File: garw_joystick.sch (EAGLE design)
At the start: 15 parts, among them IC1 TLC339D, X1 PS-05_WL, X2 PS-08_WL

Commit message: Minot stylistic fixup
Signed-off-by: Ralf Ramsauer <ralf@vmexit.de>
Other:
- note added: "Upper threshold: ~11.33V VCC - 1k3 - 22k - GND Lower threshold: ~0.67V VCC - 22k - 1k3 - GND"
- note removed: "1k3 oben 22k unten => 11.33 V 22k oben 1k3 unten => 0.67V"
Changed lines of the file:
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@@
 <grid distance="0.1" unitdist="inch" unit="inch" style="lines" multiple="1" display="no" altdistance="0.01" altunitdist="inch" altunit="inch"/>
 <layers>
-<layer number="1" name="Top" color="4" fill="1" visible="yes" active="no"/>
-<layer number="2" name="Route2" color="16" fill="1" visible="yes" active="no"/>
-<layer number="3" name="Route3" color="17" fill="1" visible="yes" active="no"/>
-<layer number="4" name="Route4" color="18" fill="1" visible="yes" active="no"/>
-<layer number="5" name="Route5" color="19" fill="1" visible="yes" active="no"/>
-<layer number="6" name="Route6" color="25" fill="1" visible="yes" active="no"/>
-<layer number="7" name="Route7" color="26" fill="1" visible="yes" active="no"/>
-<layer number="8" name="Route8" color="27" fill="1" visible="yes" active="no"/>
-<layer number="9" name="Route9" color="28" fill="1" visible="yes" active="no"/>
-<layer number="10" name="Route10" color="29" fill="1" visible="yes" active="no"/>
-<layer number="11" name="Route11" color="30" fill="1" visible="yes" active="no"/>
-<layer number="12" name="Route12" color="20" fill="1" visible="yes" active="no"/>
-<layer number="13" name="Route13" color="21" fill="1" visible="yes" active="no"/>
-<layer number="14" name="Route14" color="22" fill="1" visible="yes" active="no"/>
-<layer number="15" name="Route15" color="23" fill="1" visible="yes" active="no"/>
-<layer number="16" name="Bottom" color="1" fill="1" visible="yes" active="no"/>
-<layer number="17" name="Pads" color="2" fill="1" visible="yes" active="no"/>
-<layer number="18" name="Vias" color="2" fill="1" visible="yes" active="no"/>
-<layer number="19" name="Unrouted" color="6" fill="1" visible="yes" active="no"/>
-<layer number="20" name="Dimension" color="24" fill="1" visible="yes" active="no"/>
-<layer number="21" name="tPlace" color="7" fill="1" visible="yes" active="no"/>
-<layer number="22" name="bPlace" color="7" fill="1" visible="yes" active="no"/>
-<layer number="23" name="tOrigins" color="15" fill="1" visible="yes" active="no"/>
-<layer number="24" name="bOrigins" color="15" fill="1" visible="yes" active="no"/>
-<layer number="25" name="tNames" color="7" fill="1" visible="yes" active="no"/>
-<layer number="26" name="bNames" color="7" fill="1" visible="yes" active="no"/>
-<layer number="27" name="tValues" color="7" fill="1" visible="yes" active="no"/>
-<layer number="28" name="bValues" color="7" fill="1" visible="yes" active="no"/>
+<layer number="1" name="Top" color="4" fill="1" visible="no" active="no"/>
+<layer number="2" name="Route2" color="16" fill="1" visible="no" active="no"/>
+<layer number="3" name="Route3" color="17" fill="1" visible="no" active="no"/>
+<layer number="4" name="Route4" color="18" fill="1" visible="no" active="no"/>
+<layer number="5" name="Route5" color="19" fill="1" visible="no" active="no"/>
+<layer number="6" name="Route6" color="25" fill="1" visible="no" active="no"/>
+<layer number="7" name="Route7" color="26" fill="1" visible="no" active="no"/>
+<layer number="8" name="Route8" color="27" fill="1" visible="no" active="no"/>
+<layer number="9" name="Route9" color="28" fill="1" visible="no" active="no"/>
+<layer number="10" name="Route10" color="29" fill="1" visible="no" active="no"/>
+<layer number="11" name="Route11" color="30" fill="1" visible="no" active="no"/>
+<layer number="12" name="Route12" color="20" fill="1" visible="no" active="no"/>
+<layer number="13" name="Route13" color="21" fill="1" visible="no" active="no"/>
+<layer number="14" name="Route14" color="22" fill="1" visible="no" active="no"/>
+<layer number="15" name="Route15" color="23" fill="1" visible="no" active="no"/>
+<layer number="16" name="Bottom" color="1" fill="1" visible="no" active="no"/>
+<layer number="17" name="Pads" color="2" fill="1" visible="no" active="no"/>
+<layer number="18" name="Vias" color="2" fill="1" visible="no" active="no"/>
+<layer number="19" name="Unrouted" color="6" fill="1" visible="no" active="no"/>
+<layer number="20" name="Dimension" color="24" fill="1" visible="no" active="no"/>
+<layer number="21" name="tPlace" color="7" fill="1" visible="no" active="no"/>
+<layer number="22" name="bPlace" color="7" fill="1" visible="no" active="no"/>
+<layer number="23" name="tOrigins" color="15" fill="1" visible="no" active="no"/>
+<layer number="24" name="bOrigins" color="15" fill="1" visible="no" active="no"/>
+<layer number="25" name="tNames" color="7" fill="1" visible="no" active="no"/>
+<layer number="26" name="bNames" color="7" fill="1" visible="no" active="no"/>
+<layer number="27" name="tValues" color="7" fill="1" visible="no" active="no"/>
+<layer number="28" name="bValues" color="7" fill="1" visible="no" active="no"/>
 <layer number="29" name="tStop" color="7" fill="3" visible="no" active="no"/>
 <layer number="30" name="bStop" color="7" fill="6" visible="no" active="no"/>
@@
 <layer number="35" name="tGlue" color="7" fill="4" visible="no" active="no"/>
 <layer number="36" name="bGlue" color="7" fill="5" visible="no" active="no"/>
-<layer number="37" name="tTest" color="7" fill="1" visible="yes" active="no"/>
-<layer number="38" name="bTest" color="7" fill="1" visible="yes" active="no"/>
+<layer number="37" name="tTest" color="7" fill="1" visible="no" active="no"/>
+<layer number="38" name="bTest" color="7" fill="1" visible="no" active="no"/>
 <layer number="39" name="tKeepout" color="4" fill="11" visible="no" active="no"/>
 <layer number="40" name="bKeepout" color="1" fill="11" visible="no" active="no"/>
@@
 <layer number="44" name="Drills" color="7" fill="1" visible="no" active="no"/>
 <layer number="45" name="Holes" color="7" fill="1" visible="no" active="no"/>
-<layer number="46" name="Milling" color="3" fill="1" visible="yes" active="no"/>
-<layer number="47" name="Measures" color="7" fill="1" visible="yes" active="no"/>
-<layer number="48" name="Document" color="7" fill="1" visible="yes" active="no"/>
-<layer number="49" name="Reference" color="7" fill="1" visible="yes" active="no"/>
-<layer number="50" name="dxf" color="7" fill="1" visible="yes" active="no"/>
-<layer number="51" name="tDocu" color="7" fill="1" visible="yes" active="no"/>
-<layer number="52" name="bDocu" color="7" fill="1" visible="yes" active="no"/>
-<layer number="53" name="tGND_GNDA" color="7" fill="9" visible="yes" active="no"/>
-<layer number="54" name="bGND_GNDA" color="1" fill="9" visible="yes" active="no"/>
-<layer number="56" name="wert" color="7" fill="1" visible="yes" active="no"/>
-<layer number="57" name="tCAD" color="7" fill="1" visible="yes" active="no"/>
-<layer number="59" name="tCarbon" color="7" fill="1" visible="yes" active="no"/>
-<layer number="60" name="bCarbon" color="7" fill="1" visible="yes" active="no"/>
+<layer number="46" name="Milling" color="3" fill="1" visible="no" active="no"/>
+<layer number="47" name="Measures" color="7" fill="1" visible="no" active="no"/>
+<layer number="48" name="Document" color="7" fill="1" visible="no" active="no"/>
+<layer number="49" name="Reference" color="7" fill="1" visible="no" active="no"/>
+<layer number="50" name="dxf" color="7" fill="1" visible="no" active="no"/>
+<layer number="51" name="tDocu" color="7" fill="1" visible="no" active="no"/>
+<layer number="52" name="bDocu" color="7" fill="1" visible="no" active="no"/>
+<layer number="53" name="tGND_GNDA" color="7" fill="9" visible="no" active="no"/>
+<layer number="54" name="bGND_GNDA" color="1" fill="9" visible="no" active="no"/>
+<layer number="56" name="wert" color="7" fill="1" visible="no" active="no"/>
+<layer number="57" name="tCAD" color="7" fill="1" visible="no" active="no"/>
+<layer number="59" name="tCarbon" color="7" fill="1" visible="no" active="no"/>
+<layer number="60" name="bCarbon" color="7" fill="1" visible="no" active="no"/>
 <layer number="88" name="SimResults" color="9" fill="1" visible="yes" active="yes"/>
 <layer number="89" name="SimProbes" color="9" fill="1" visible="yes" active="yes"/>
@@
 <sheet>
 <plain>
-<text x="66.04" y="101.6" size="5.08" layer="150">1k3 oben
-22k unten
-=&gt; 11.33 V
-22k oben
-1k3 unten
-=&gt; 0.67V</text>
+<text x="104.14" y="137.16" size="1.778" layer="95">Upper threshold: ~11.33V
+VCC - 1k3 - 22k - GND
+Lower threshold: ~0.67V
+VCC - 22k - 1k3 - GND</text>
 </plain>
 <instances>

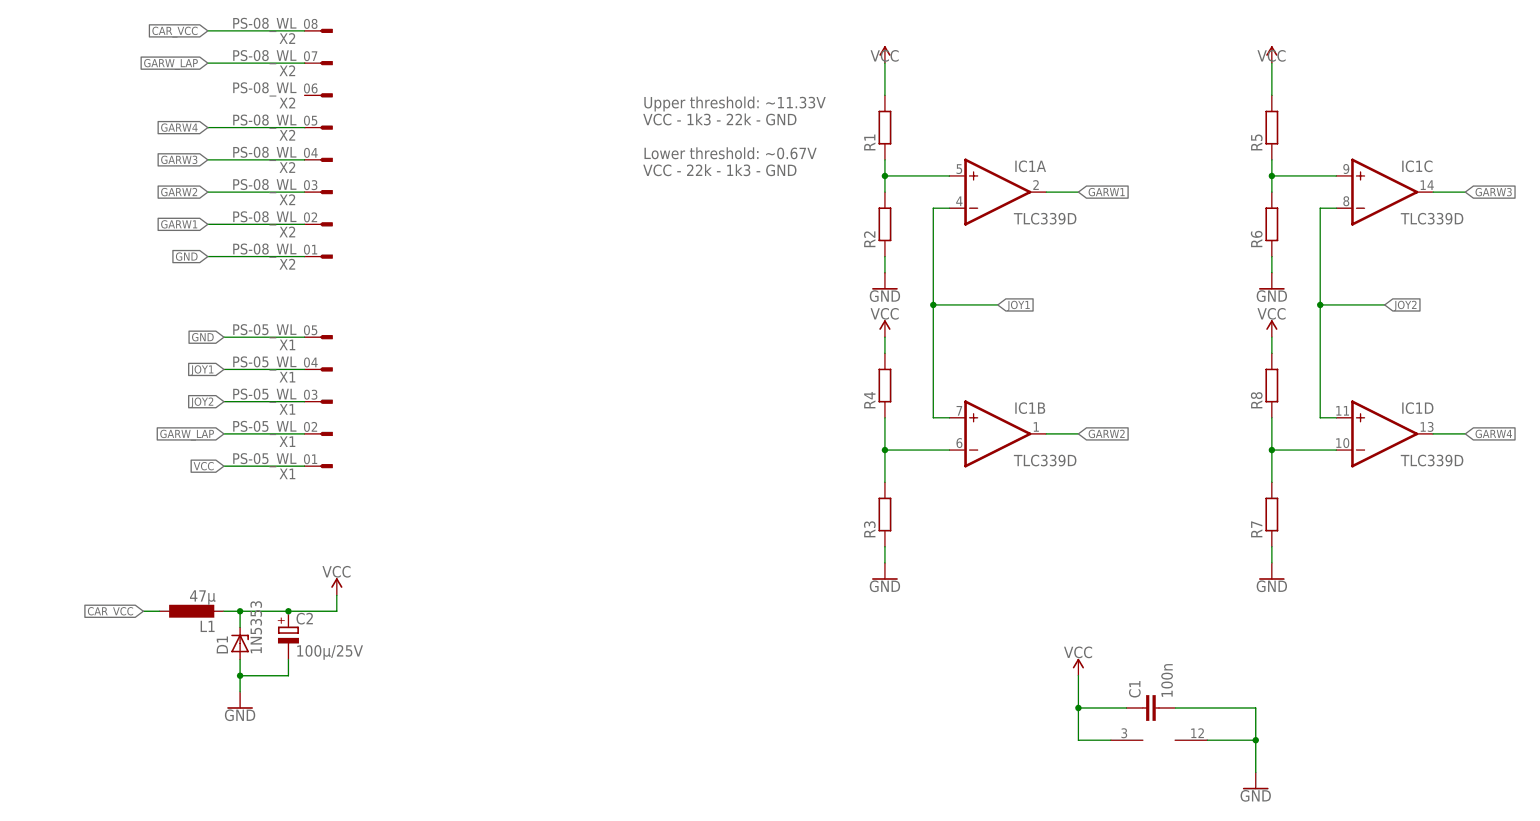
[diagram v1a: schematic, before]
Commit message: Add low pass filters
Signed-off-by: Ralf Ramsauer <ralf@vmexit.de>
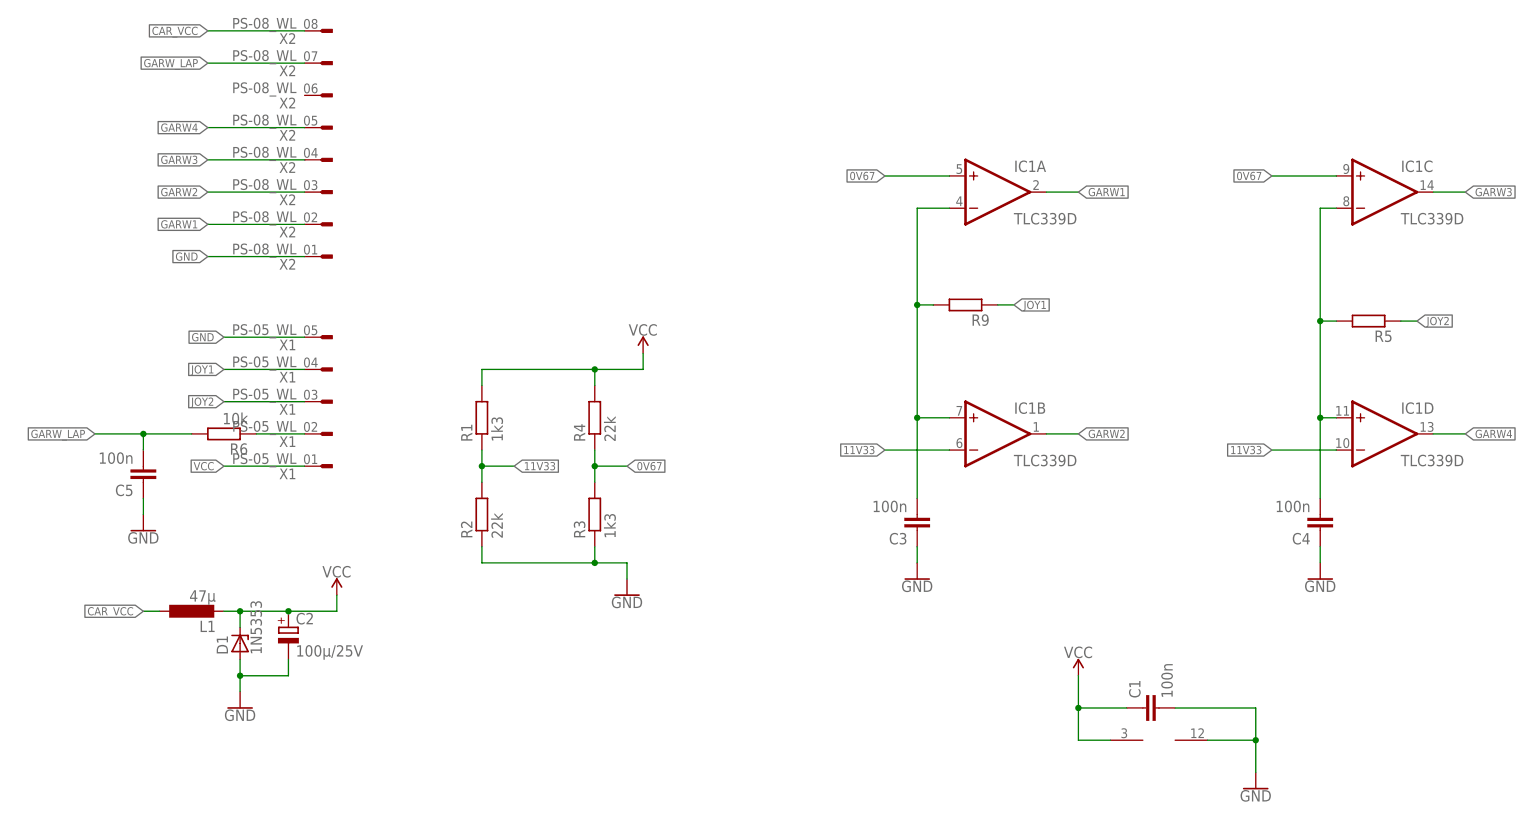
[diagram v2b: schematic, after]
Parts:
- removed R7, R8: (no value), rcl:R-EU_M0805
- added C3, C4, C5: 100n, rcl:C-EUC0805
- added R9: (no value), rcl:R-EU_M0805
- R1, R3: value (none) -> 1k3
- R2, R4: value (none) -> 22k
- R6: value (none) -> 10k
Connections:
- removed net N$2: IC1B.-IN, R3.2, R4.1
- removed net N$3: IC1C.+IN, R5.1, R6.2
- removed net N$4: IC1D.-IN, R7.2, R8.1
- new net 0V67: IC1A.+IN, IC1C.+IN, R3.2, R4.1
- new net 11V33: IC1B.-IN, IC1D.-IN, R1.1, R2.2
- new net N$5: C4.2, IC1C.-IN, IC1D.+IN, R5.2
- new net N$8: C3.2, IC1A.-IN, IC1B.+IN, R9.2
- net GARW_LAP: now also C5.2, R6.2; no longer X1G$2.P$1
- net GND: now also C3.1, C4.1, C5.1; no longer R6.1, R7.1
- net JOY1: now also R9.1; no longer IC1A.-IN, IC1B.+IN
- net JOY2: now also R5.1; no longer IC1C.-IN, IC1D.+IN
- net N$1: now also R6.1, X1G$2.P$1; no longer IC1A.+IN, R1.1, R2.2
- net VCC: no longer R5.2, R8.2
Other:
- note removed: "Upper threshold: ~11.33V VCC - 1k3 - 22k - GND Lower threshold: ~0.67V VCC - 22k - 1k3 - GND"
- moved on the sheet: R1, R2, R3, R4, R5, R6

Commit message: Flip 0V6 and 11V3 net
They were placed in the opposite way.

Signed-off-by: Ralf Ramsauer <ralf@vmexit.de>
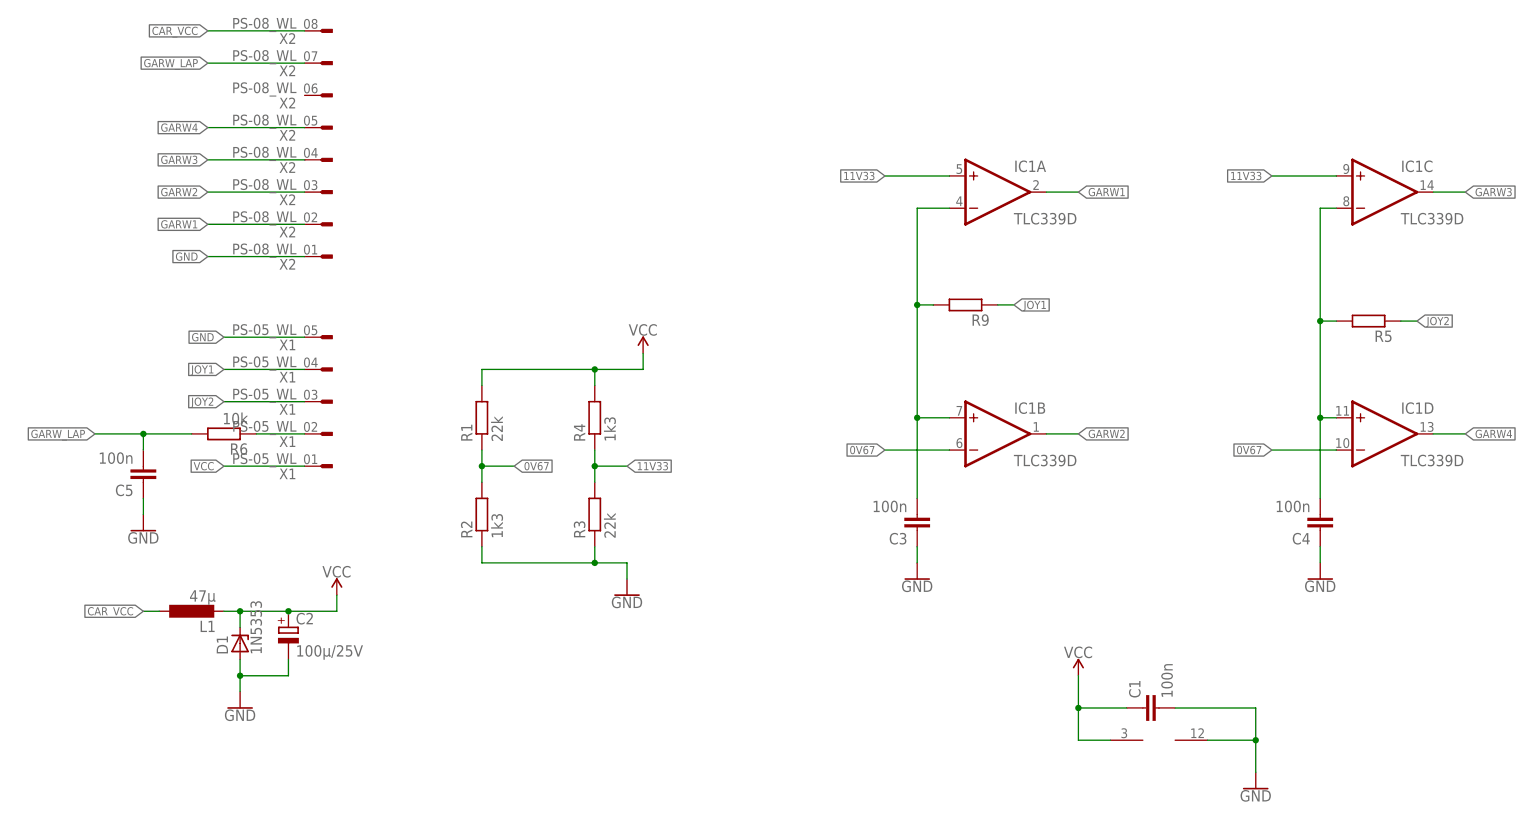
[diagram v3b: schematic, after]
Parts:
- R1, R3: value 1k3 -> 22k
- R2, R4: value 22k -> 1k3
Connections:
- net 0V67: now also IC1B.-IN, IC1D.-IN, R1.1, R2.2; no longer IC1A.+IN, IC1C.+IN, R3.2, R4.1
- net 11V33: now also IC1A.+IN, IC1C.+IN, R3.2, R4.1; no longer IC1B.-IN, IC1D.-IN, R1.1, R2.2
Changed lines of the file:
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@@
 <part name="SUPPLY1" library="SparkFun-PowerSymbols" library_urn="urn:adsk.eagle:library:530" deviceset="VCC" device=""/>
 <part name="GND1" library="SparkFun-PowerSymbols" library_urn="urn:adsk.eagle:library:530" deviceset="GND" device=""/>
-<part name="R1" library="rcl" library_urn="urn:adsk.eagle:library:334" deviceset="R-EU_" device="M0805" package3d_urn="urn:adsk.eagle:package:23556/1" value="1k3"/>
-<part name="R2" library="rcl" library_urn="urn:adsk.eagle:library:334" deviceset="R-EU_" device="M0805" package3d_urn="urn:adsk.eagle:package:23556/1" value="22k"/>
-<part name="R3" library="rcl" library_urn="urn:adsk.eagle:library:334" deviceset="R-EU_" device="M0805" package3d_urn="urn:adsk.eagle:package:23556/1" value="1k3"/>
-<part name="R4" library="rcl" library_urn="urn:adsk.eagle:library:334" deviceset="R-EU_" device="M0805" package3d_urn="urn:adsk.eagle:package:23556/1" value="22k"/>
+<part name="R1" library="rcl" library_urn="urn:adsk.eagle:library:334" deviceset="R-EU_" device="M0805" package3d_urn="urn:adsk.eagle:package:23556/1" value="22k"/>
+<part name="R2" library="rcl" library_urn="urn:adsk.eagle:library:334" deviceset="R-EU_" device="M0805" package3d_urn="urn:adsk.eagle:package:23556/1" value="1k3"/>
+<part name="R3" library="rcl" library_urn="urn:adsk.eagle:library:334" deviceset="R-EU_" device="M0805" package3d_urn="urn:adsk.eagle:package:23556/1" value="22k"/>
+<part name="R4" library="rcl" library_urn="urn:adsk.eagle:library:334" deviceset="R-EU_" device="M0805" package3d_urn="urn:adsk.eagle:package:23556/1" value="1k3"/>
 <part name="SUPPLY3" library="SparkFun-PowerSymbols" library_urn="urn:adsk.eagle:library:530" deviceset="VCC" device=""/>
 <part name="GND3" library="SparkFun-PowerSymbols" library_urn="urn:adsk.eagle:library:530" deviceset="GND" device=""/>
@@
 </segment>
 </net>
-<net name="11V33" class="0">
+<net name="0V67" class="0">
 <segment>
 <pinref part="R1" gate="G$1" pin="1"/>
@@
 </segment>
 </net>
-<net name="0V67" class="0">
+<net name="11V33" class="0">
 <segment>
 <pinref part="R4" gate="G$1" pin="1"/>
